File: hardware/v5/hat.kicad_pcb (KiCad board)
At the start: 2 copper layers, 65 x 56 mm, 5 parts, among them J1 GPIO

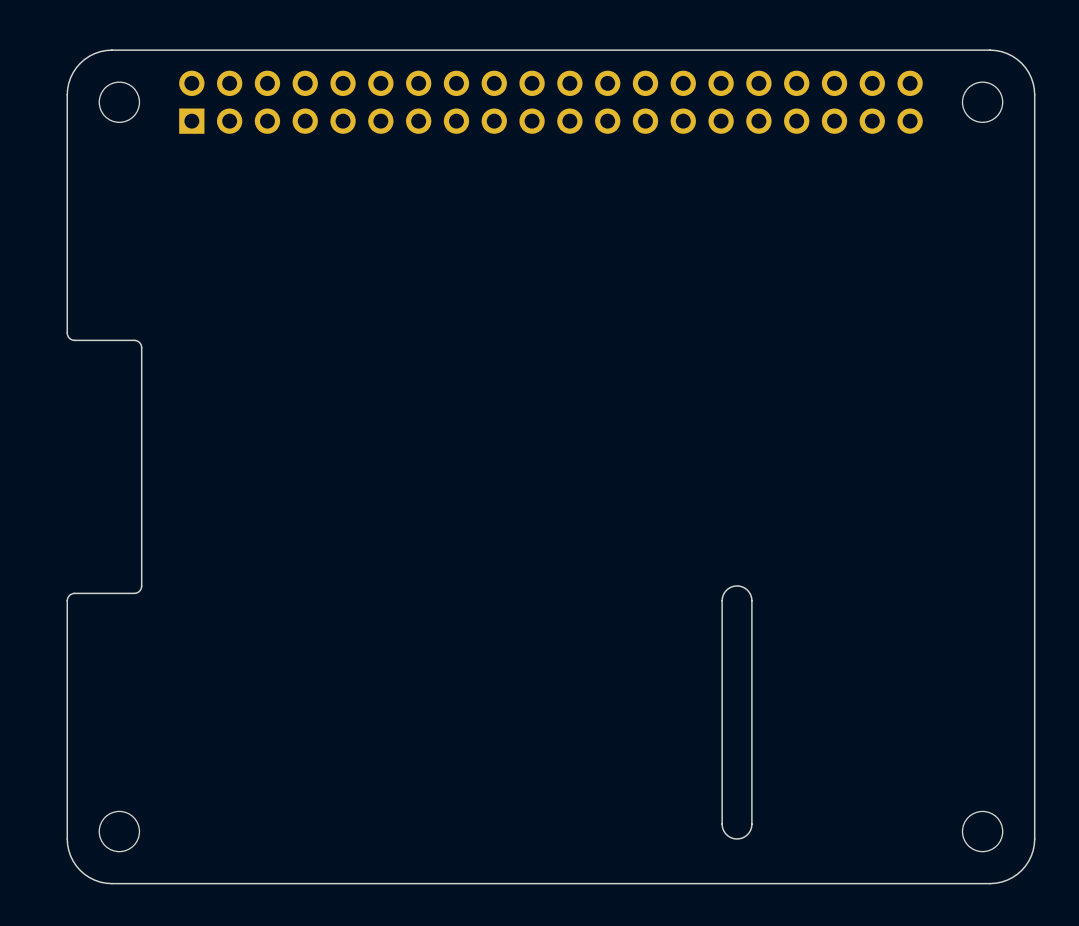
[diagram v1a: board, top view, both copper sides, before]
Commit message: v5: import/reimplement parport design on template
Problem: template board is still blank.

Adjust board edge to handle SMT header and add cutout for pi5 camera/
display FFC connectors.  For GPIO connector, use existing kicad 8 Harwin
M20 series footprint but adjust the pinout for top of board pi GPIO,
and adjust position since centroid moved from THT pin 1 to SMT centroid.
Add keepout for pi5 PoE like the existing one for pi4.

Import the SN74LVC16128 symbol from the v4 board.  Orient the chip
as before for best routing but aim for tighter traces this time.
Add bypass caps to all power inputs for good measure.  Chip capacitors
and resistors are shrunk from 0805 to 0603 in this revision.  Allow the
cable VCC to be jumpered to either 5V or 3V3 per the spec sheet.

Move the EEPROM to the east end of the board for more direct routing.
Add a strong 1K pull-up to the template's WP jumper per the HAT+ spec.
Orient the chip the same direction as the SN74LVC16128 to avoid confusion.

Add the DB-25 right-angle 2x13 header on the west end as before.
This time, use a custom header footprint so the DB-25 pin numbers can
be mirrored on the header.  Also, add a board cutout to improve insertion
ergonmics if the right angle header is used.

Implement the GPIO reassignments proposed in #67.  This should allow
I2C, UART0, and PWM0 to be used in stacked HATs.

Add a Sparkfun Qwiic connector to allow I2C expansion that way as well.
See: https://www.sparkfun.com/qwiic.

Put the official HAT+ logo on the board since this board complies with
https://datasheets.raspberrypi.com/hat/hat-plus-specification.pdf.
The logo image was provided via email along with marking guidelines.
Use the minimum 2.25mm height specified in the guidelines.

Add some helpful notes and the DB-25 pinout to the board silkscreen.
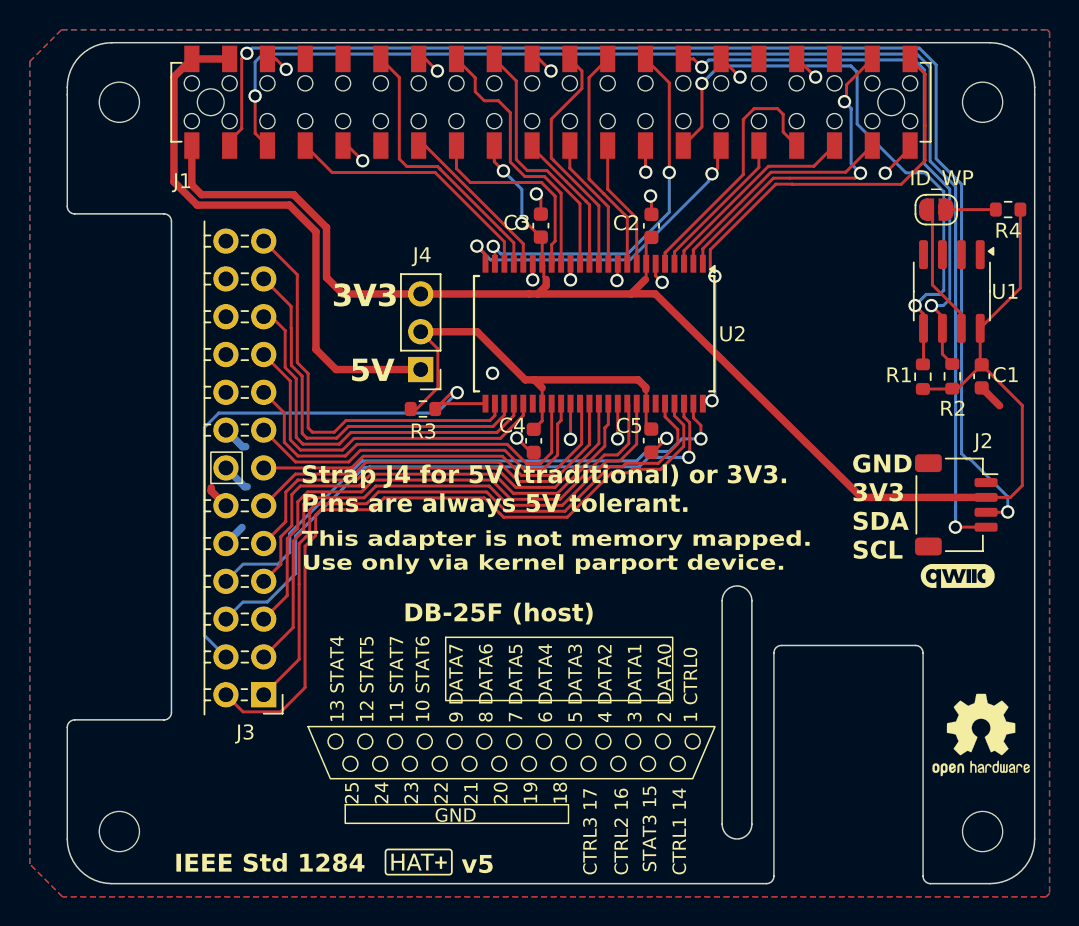
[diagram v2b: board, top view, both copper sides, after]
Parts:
- added C1: 100n, Capacitor_SMD:C_0603_1608Metric, F.Cu at (161.4, 65.9)
- added C2: 100n, Capacitor_SMD:C_0603_1608Metric, F.Cu at (139.2, 55.8)
- added C3: 100n, Capacitor_SMD:C_0603_1608Metric, F.Cu at (131.8, 55.8)
- added C4: 100n, Capacitor_SMD:C_0603_1608Metric, F.Cu at (131.3, 70.2)
- added C5: 100n, Capacitor_SMD:C_0603_1608Metric, F.Cu at (139.2, 70.2)
- added G***: LOGO, lib:qwiic_5mm, F.Cu at (159.8, 79.3)
- added G***: LOGO, lib:HAT_plus_logo, F.Cu at (123.6, 98.5)
- added J2: Qwiic, Connector_JST:JST_SH_SM04B-SRSS-TB_1x04-1MP_P1.00mm_Horizontal, F.Cu at (159.7, 74.5)
- added J3: DB25 header, lib:DB25_header_2x13_P2.54mm_horizontal, F.Cu at (113.2, 87.3)
- added J4: V select, Connector_PinHeader_2.54mm:PinHeader_1x03_P2.54mm_Vertical, F.Cu at (123.8, 65.5)
- added JP1: ID_WP, Jumper:SolderJumper-2_P1.3mm_Open_RoundedPad1.0x1.5mm, F.Cu at (158.4, 54.7)
- added R1: 3.9k, Resistor_SMD:R_0603_1608Metric, F.Cu at (157.5, 65.9)
- added R2: 3.9k, Resistor_SMD:R_0603_1608Metric, F.Cu at (159.5, 65.9)
- added R3: 1.4k, Resistor_SMD:R_0603_1608Metric, F.Cu at (123.9, 68.1)
- added R4: 1k, Resistor_SMD:R_0603_1608Metric, F.Cu at (163.2, 54.7)
- added REF**: parport_pinout, lib:parport_pinout, F.Cu at (116.2, 89.5)
- added REF**: OSHW-Logo2_7.3x6mm_SilkScreen, Symbol:OSHW-Logo2_7.3x6mm_SilkScreen, F.Cu at (161.4, 90.0)
- added U1: CAT24C256, Package_SO:SOIC-8_3.9x4.9mm_P1.27mm, F.Cu at (159.4, 60.2)
- added U2: SN74LVC161284DLR, Package_SO:SSOP-48_7.5x15.9mm_P0.635mm, F.Cu at (135.4, 63.0)
- J1: footprint Connector_PinSocket_2.54mm:PinSocket_2x20_P2.54mm_Vertical -> lib:Harwin_M20-7812045_2x20_P2.54mm_Vertical; moved to F.Cu
- moved J1 24.2 mm to (132.5, 47.5), turned to 90 degrees
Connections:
- net /GPIO16 renamed /GPIO16/CTS0
- net /GPIO17 renamed /GPIO17/RTS0
- J1 pad 12: /GPIO18/PCM.CLK -> /GPIO18
- J1 pad 19: /GPIO10/SPI0.MOSI -> /GPIO10
- J1 pad 21: /GPIO9/SPI0.MISO -> /GPIO9
- J1 pad 23: /GPIO11/SPI0.SCLK -> /GPIO11
- J1 pad 24: /GPIO8/SPI0.CE0 -> /GPIO8
- J1 pad 26: /GPIO7/SPI0.CE1 -> /GPIO7
- J1 pad 3: /GPIO2/SDA1 -> /GPIO2/SDA
- J1 pad 33: /GPIO13/PWM1 -> /GPIO13
- J1 pad 35: /GPIO19/PCM.FS -> /GPIO19
- J1 pad 38: /GPIO20/PCM.DIN -> /GPIO20
- J1 pad 40: /GPIO21/PCM.DOUT -> /GPIO21
- J1 pad 5: /GPIO3/SCL1 -> /GPIO3/SCL
- J1 pad 7: /GPIO4/GPCLK0 -> /GPIO4
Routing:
- net +3V3: track 0.00 -> 111.6 mm, vias 0 -> 2
- net /GPIO2/SDA: track 0.00 -> 87.2 mm, vias 0 -> 2
- net /GPIO3/SCL: track 0.00 -> 85.6 mm, vias 0 -> 2
- net /CONTROL1: track 0.00 -> 49.2 mm
- net /CONTROL0: track 0.00 -> 44.3 mm
- net /CONTROL2: track 0.00 -> 40.9 mm, vias 0 -> 1
- net /ID_SDA: track 0.00 -> 40.4 mm, vias 0 -> 2
- net /STATUS3: track 0.00 -> 39.4 mm, vias 0 -> 1
- net /DATA0: track 0.00 -> 39.2 mm
- net /CONTROL3: track 0.00 -> 39.2 mm, vias 0 -> 1
- net /ID_SCL: track 0.00 -> 39.1 mm, vias 0 -> 2
- net GND: track 0.00 -> 38.7 mm, vias 0 -> 19
- net +5V: track 0.00 -> 37.7 mm
- net /DATA1: track 0.00 -> 36.5 mm
- net /GPIO21: track 0.00 -> 35.2 mm, vias 0 -> 2
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- added copper zone on B.Cu, net GND
- added copper zone on F.Cu, net GND
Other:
- board size 65 x 56 mm -> 65 x 56.5 mm
- board text added: "(C)2024 WorlickWerx, LLC"
- board text added: "3V3"
- board text added: "5V"
- board text added: "DB-25F (host)"
- board text added: "GND 3V3 SDA SCL"
- board text added: "IEEE Std 1284"
- board text added: "Software and design files: https://github.com/worlickwerx/pi-parport/"
- board text added: "Strap J4 for 5V (traditional) or 3V3. Pins are always 5V tolerant."
- board text added: "This adapter is not memory mapped. Use only via kernel parport device."
- board text added: "v5"
- board text removed: "CAMERA (OPTIONAL)"
- board text removed: "DISPLAY (OPTIONAL)"
- board text removed: "Extend PCB edge 0.5mm if using SMT header"
